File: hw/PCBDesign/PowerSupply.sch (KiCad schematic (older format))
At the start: 37 parts, among them J2 USB_B_Micro, J3 ExtBatt, U7 BQ24074RGT, U8 AMS1117-3.3

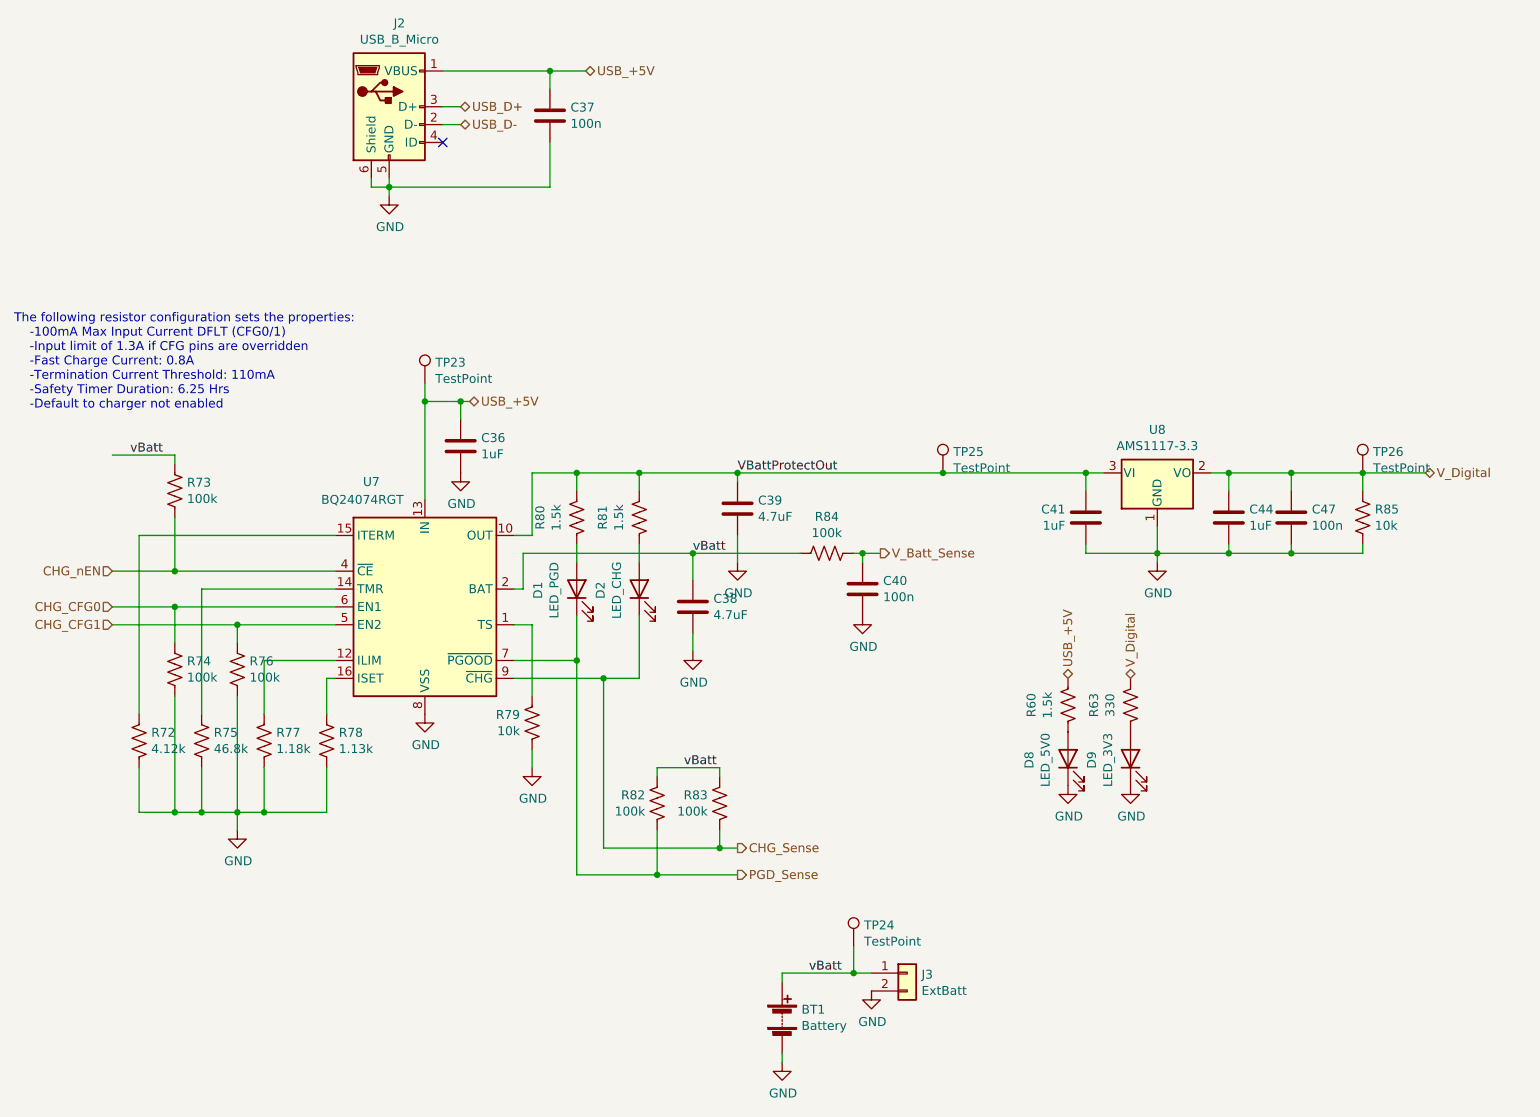
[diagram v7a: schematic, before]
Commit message: Adjust components for lowest build cost
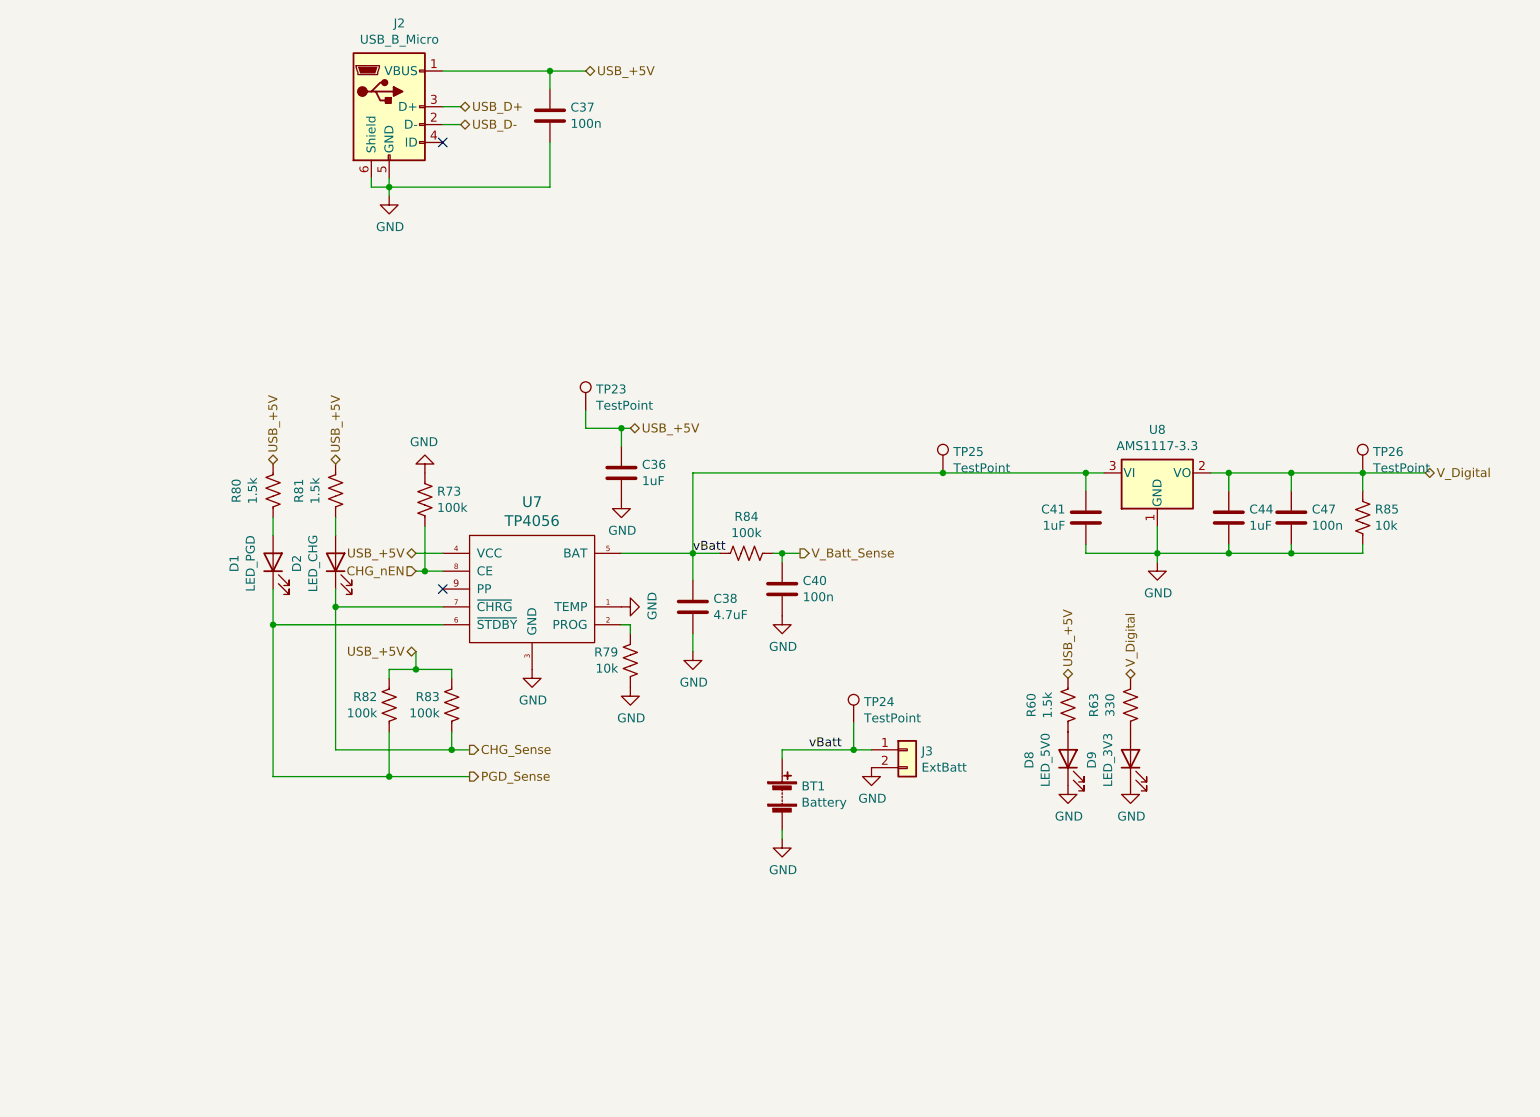
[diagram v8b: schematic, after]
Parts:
- removed C39: 4.7uF, Capacitor_SMD:C_0805_2012Metric, symbol Device:C
- removed R72: 4.12k, Resistor_SMD:R_0402_1005Metric, symbol Device:R_US
- removed R74, R76: 100k, Resistor_SMD:R_0402_1005Metric, symbol Device:R_US
- removed R75: 46.8k, Resistor_SMD:R_0402_1005Metric, symbol Device:R_US
- removed R77: 1.18k, Resistor_SMD:R_0402_1005Metric, symbol Device:R_US
- removed R78: 1.13k, Resistor_SMD:R_0402_1005Metric, symbol Device:R_US
- removed U7: BQ24074RGT, Package_DFN_QFN:VQFN-16-1EP_3x3mm_P0.5mm_EP1.6x1.6mm, symbol Battery_Management:BQ24074RGT
- added U7: TP4056, PMIC:TP4056_SOP-8-PP, symbol tp4056:TP4056
- D8: LCSC C72041 -> C72043
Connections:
- net CHG_Sense: now also U7.7 (~CHRG)
- net CHG_nEN: now also U7.8 (CE)
- net GND: now also R73.2, U7.1 (TEMP), U7.3 (GND)
- net PGD_Sense: now also U7.6 (~STDBY)
- net USB_+5V: now also R80.2, R81.2, R82.2, R83.2, U7.4 (VCC)
- net vBatt: now also C41.2, TP25.1, U8.3 (VI), U7.5 (BAT); no longer R73.2, R82.2, R83.2
- net at R79.2: now also U7.2 (PROG)
- removed net VBattProtectOut: C41.2, R80.2, R81.2, TP25.1, U8.3 (VI)
- no-connect marks 1 -> 2
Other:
- note removed: "The following resistor configuration sets the properties:\n -100mA Max Input Current DFLT (CFG0/1)\n -Input limit of 1.3A if CFG pins are overridden\n -Fast Charge Current: 0.8A\n -Termination Current Threshold: 110mA\n -Safety Timer Duration: 6.25 Hrs\n -Default to charger not enabled"
- moved on the sheet: BT1, C36, C40, D1, D2, J3, R73, R79, R80, R81, R82, R83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
